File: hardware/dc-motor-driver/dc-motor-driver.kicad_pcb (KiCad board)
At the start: 2 copper layers, 73 parts, among them J1 VCC, J10 IMODE, J11 MOT, J12 IMODE, J13 MOT, J2 IMODE, J3 MOT, J4 IMODE, J5 MOT, J6 IMODE, J7 MOT, J8 IMODE, J9 MOT, U1 DRV8874PWPR, U2 DRV8874PWPR, U3 DRV8874PWPR, U4 DRV8874PWPR, U5 DRV8874PWPR, U6 DRV8874PWPR

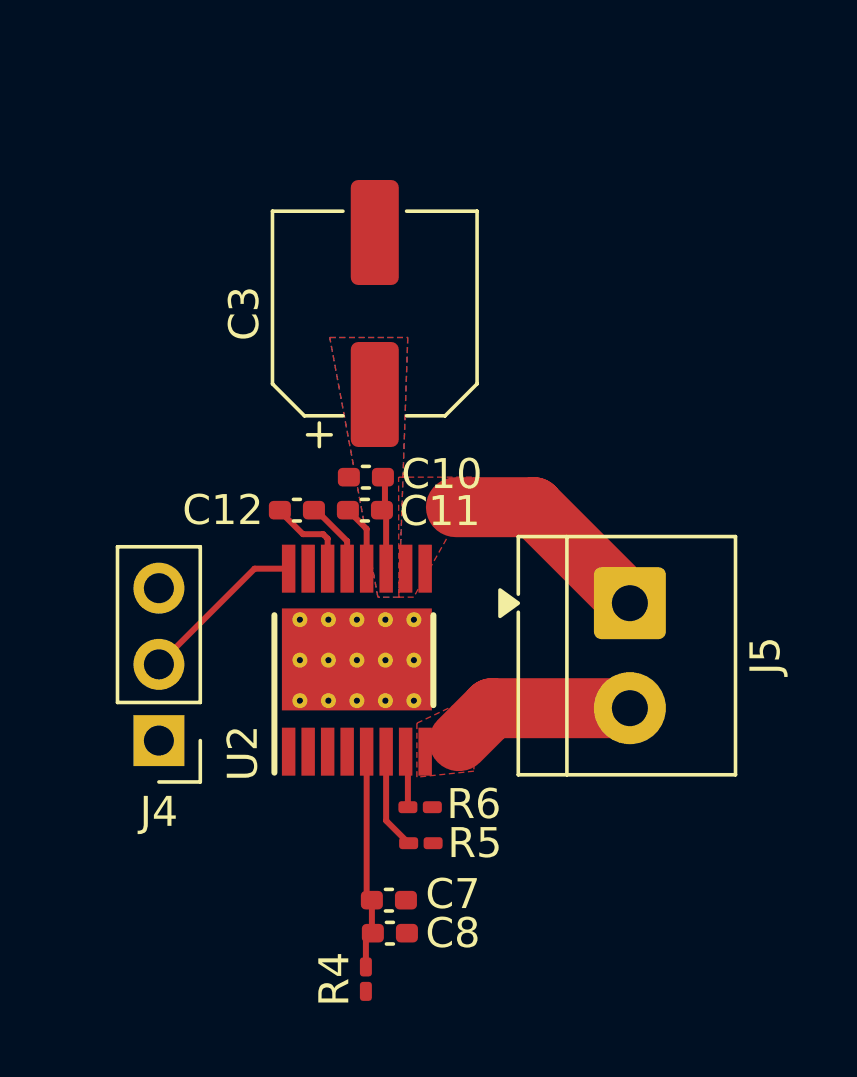
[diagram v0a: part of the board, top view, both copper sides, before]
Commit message: Replaced large current traces for copper pours and tweaked placement of components
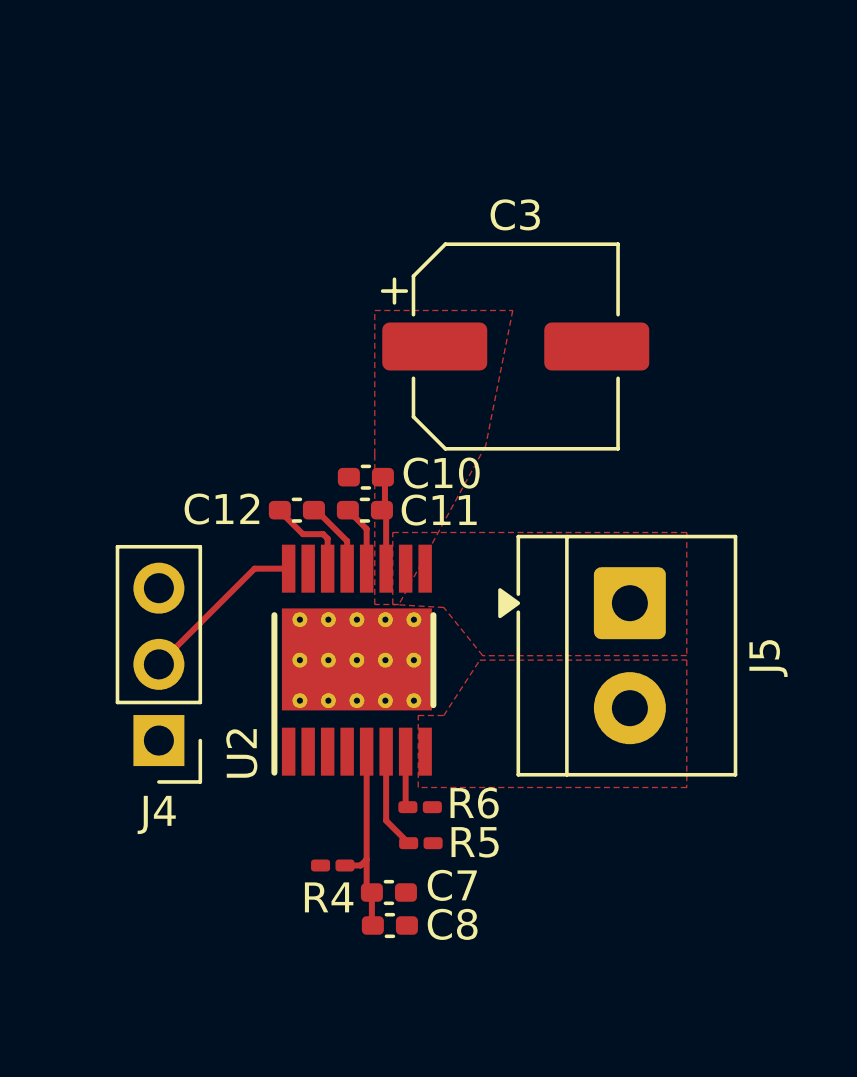
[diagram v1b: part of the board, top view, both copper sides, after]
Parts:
- moved C3 4.83 mm to (169.8, 77.5), turned to 0 degrees
- moved R4 3.95 mm to (163.7, 94.8), turned to 0 degrees
- moved C8 0.26 mm to (165.6, 96.8)
- moved C7 0.26 mm to (165.6, 95.7)
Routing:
- net Net-(J5-Pin_1): track 7.13 -> 0.00 mm
- net Net-(J5-Pin_2): track 6.16 -> 0.00 mm
- removed copper zone on B.Cu, net VCC

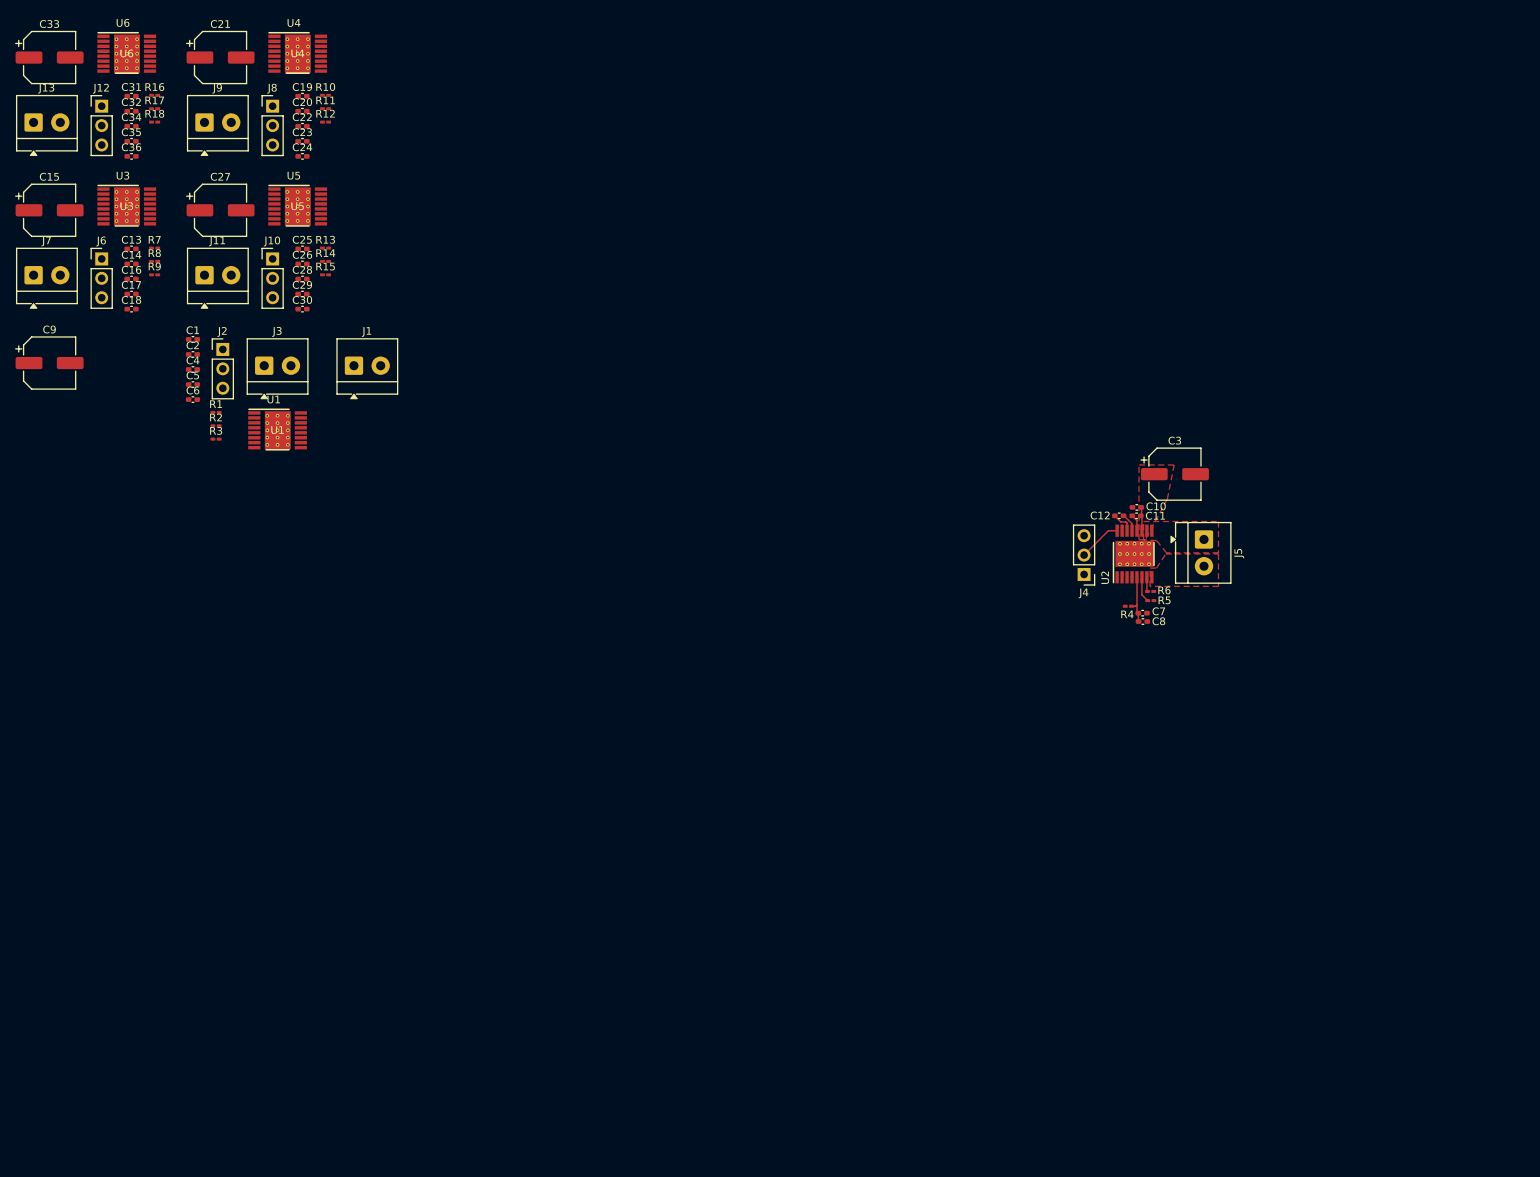
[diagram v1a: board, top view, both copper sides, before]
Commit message: feat: WIP PCB layout
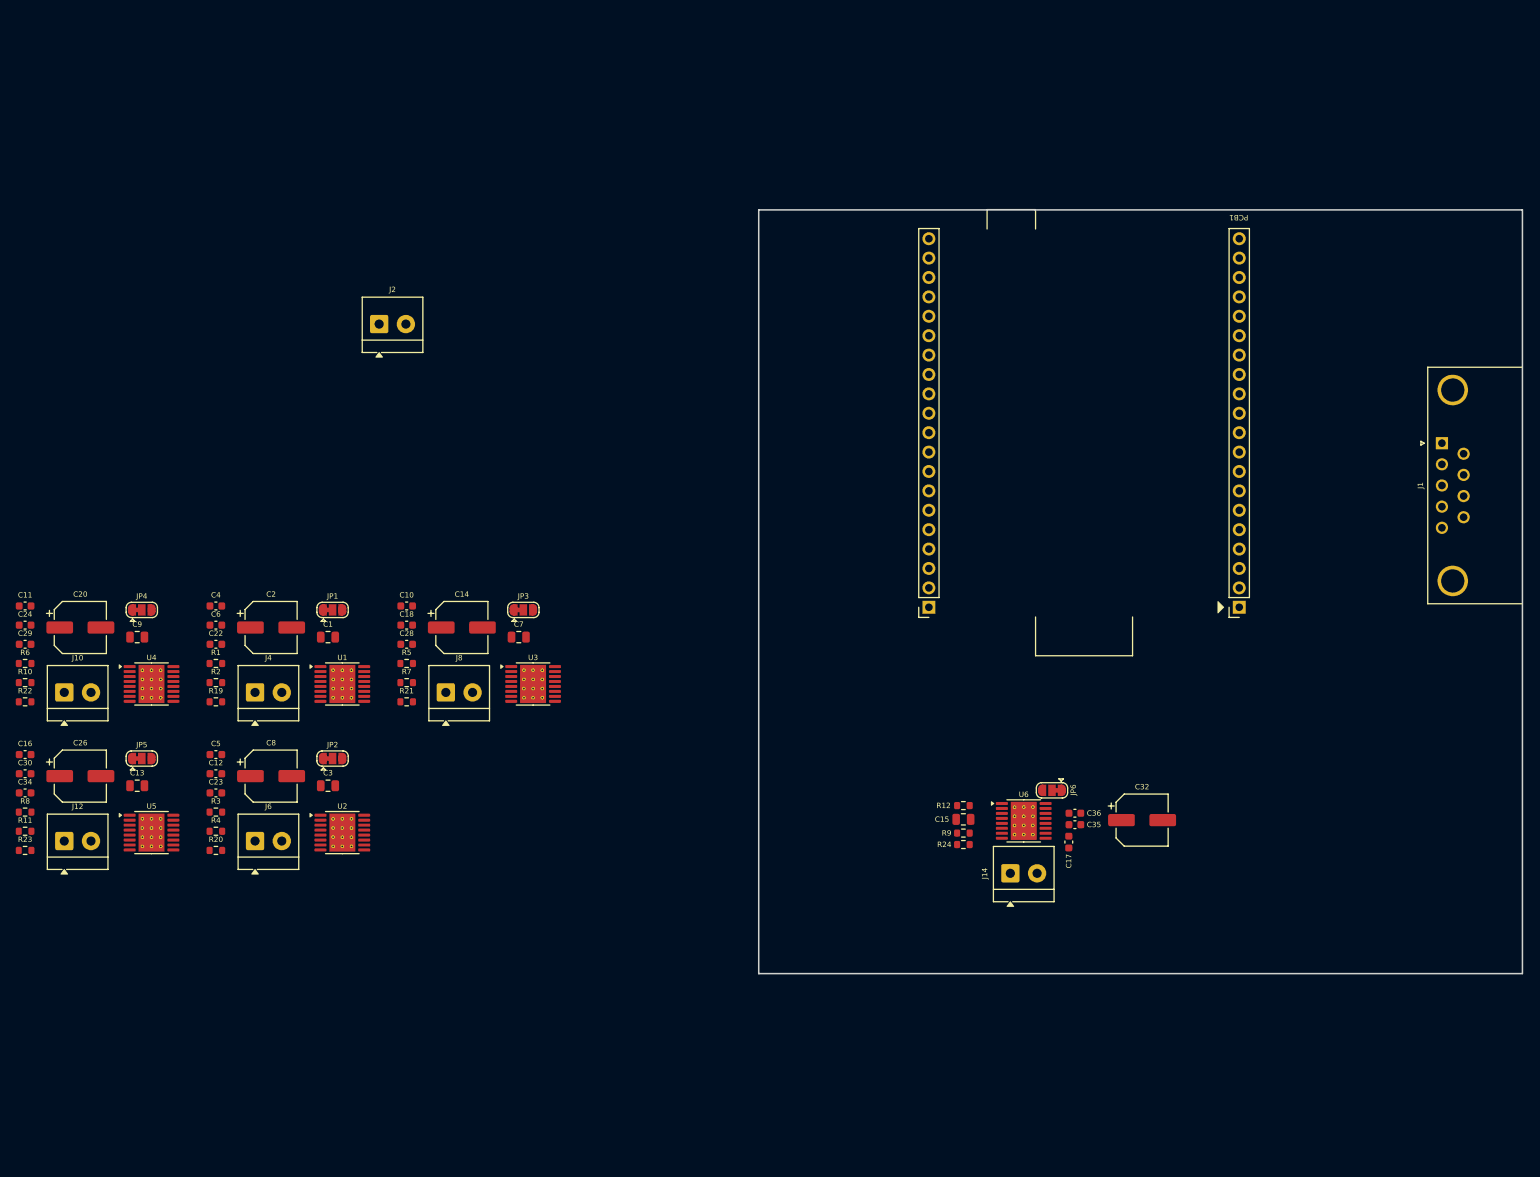
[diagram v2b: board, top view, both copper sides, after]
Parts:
- removed C19, C25, C31: 0.1uF, Capacitor_SMD:C_0402_1005Metric_Pad0.74x0.62mm_HandSolder
- removed C21, C27, C33: 100uF, Capacitor_SMD:CP_Elec_6.3x7.7
- removed J11, J13, J3, J5, J7, J9: MOT, TerminalBlock_4Ucon:TerminalBlock_4Ucon_1x02_P3.50mm_Horizontal
- removed R13, R16: 4.7k, Resistor_SMD:R_0201_0603Metric_Pad0.64x0.40mm_HandSolder
- removed R14, R17: 2.2k, Resistor_SMD:R_0201_0603Metric_Pad0.64x0.40mm_HandSolder
- removed R15, R18: 20k, Resistor_SMD:R_0201_0603Metric_Pad0.64x0.40mm_HandSolder
- added J14: MOT, TerminalBlock_4Ucon:TerminalBlock_4Ucon_1x02_P3.50mm_Horizontal, F.Cu at (148.2, 129.8)
- added JP1: Jumper_3_Bridged12, Jumper:SolderJumper-3_P1.3mm_Bridged12_RoundedPad1.0x1.5mm, F.Cu at (59.5, 95.3)
- added JP2: Jumper_3_Bridged12, Jumper:SolderJumper-3_P1.3mm_Bridged12_RoundedPad1.0x1.5mm, F.Cu at (59.5, 114.7)
- added JP3: Jumper_3_Bridged12, Jumper:SolderJumper-3_P1.3mm_Bridged12_RoundedPad1.0x1.5mm, F.Cu at (84.5, 95.3)
- added JP4: Jumper_3_Bridged12, Jumper:SolderJumper-3_P1.3mm_Bridged12_RoundedPad1.0x1.5mm, F.Cu at (34.5, 95.3)
- added JP5: Jumper_3_Bridged12, Jumper:SolderJumper-3_P1.3mm_Bridged12_RoundedPad1.0x1.5mm, F.Cu at (34.5, 114.7)
- added JP6: Jumper_3_Bridged12, Jumper:SolderJumper-3_P1.3mm_Bridged12_RoundedPad1.0x1.5mm, F.Cu at (153.7, 118.9)
- added PCB1: Smol Brain Board, Project PCB:Smol_Brain_Board, F.Cu at (157.9, 70.8)
- added R19: 20k, Resistor_SMD:R_0603_1608Metric, F.Cu at (44.2, 107.3)
- added R20: 20k, Resistor_SMD:R_0603_1608Metric, F.Cu at (44.2, 126.8)
- added R21: 20k, Resistor_SMD:R_0603_1608Metric, F.Cu at (69.2, 107.3)
- added R22: 20k, Resistor_SMD:R_0603_1608Metric, F.Cu at (19.2, 107.3)
- added R23: 20k, Resistor_SMD:R_0603_1608Metric, F.Cu at (19.2, 126.8)
- added R24: 20k, Resistor_SMD:R_0603_1608Metric, F.Cu at (142.1, 126.0)
- C1, C13, C7: value 0.1uF -> 10u; footprint Capacitor_SMD:C_0402_1005Metric_Pad0.74x0.62mm_HandSolder -> Capacitor_SMD:C_0805_2012Metric
- C10, C11, C16, C17, C22, C23, C28, C29, C34, C35, C4, C5: value 0.1uF -> 100n; footprint Capacitor_SMD:C_0402_1005Metric_Pad0.74x0.62mm_HandSolder -> Capacitor_SMD:C_0603_1608Metric
- C12, C18, C24, C30, C36, C6: value 0.022uF -> 22n; footprint Capacitor_SMD:C_0402_1005Metric_Pad0.74x0.62mm_HandSolder -> Capacitor_SMD:C_0603_1608Metric
- C14, C2, C20, C26, C32, C8: value 10uF -> 100u; footprint Capacitor_SMD:C_0402_1005Metric_Pad0.74x0.62mm_HandSolder -> Capacitor_SMD:CP_Elec_6.3x7.7
- C15, C3, C9: value 100uF -> 10u; footprint Capacitor_SMD:CP_Elec_6.3x7.7 -> Capacitor_SMD:C_0805_2012Metric
- J1: value VCC -> DE9; footprint TerminalBlock_4Ucon:TerminalBlock_4Ucon_1x02_P3.50mm_Horizontal -> THT:A-DF_09_A_KG-T2S
- J10, J12, J4, J6, J8: value IMODE -> MOT; footprint Connector_PinHeader_2.54mm:PinHeader_1x03_P2.54mm_Vertical -> TerminalBlock_4Ucon:TerminalBlock_4Ucon_1x02_P3.50mm_Horizontal
- J2: value IMODE -> VCC; footprint Connector_PinHeader_2.54mm:PinHeader_1x03_P2.54mm_Vertical -> TerminalBlock_4Ucon:TerminalBlock_4Ucon_1x02_P3.50mm_Horizontal
- R1, R10, R4, R7: value 4.7k -> 10k; footprint Resistor_SMD:R_0201_0603Metric_Pad0.64x0.40mm_HandSolder -> Resistor_SMD:R_0603_1608Metric
- R11: value 2.2k -> 10k; footprint Resistor_SMD:R_0201_0603Metric_Pad0.64x0.40mm_HandSolder -> Resistor_SMD:R_0603_1608Metric
- R12: value 20k -> 10k; footprint Resistor_SMD:R_0201_0603Metric_Pad0.64x0.40mm_HandSolder -> Resistor_SMD:R_0603_1608Metric
- R2, R5, R8: value 2.2k -> 2k2; footprint Resistor_SMD:R_0201_0603Metric_Pad0.64x0.40mm_HandSolder -> Resistor_SMD:R_0603_1608Metric
- R3, R6, R9: value 20k -> 2k2; footprint Resistor_SMD:R_0201_0603Metric_Pad0.64x0.40mm_HandSolder -> Resistor_SMD:R_0603_1608Metric
- U1, U2, U3, U4, U5, U6: footprint Package_DFN_QFN:DRV8874PWPR -> Package_SO:HTSSOP-16-1EP_4.4x5mm_P0.65mm_EP3.4x5mm_Mask2.66x2.46mm_ThermalVias
- moved C32 161.6 mm to (165.5, 122.8)
- moved U6 154.5 mm to (150.0, 122.9)
- moved C35 152.5 mm to (156.7, 123.4)
- moved C36 150.5 mm to (156.7, 121.9)
- moved R6 147.7 mm to (19.2, 102.3)
- moved C11 146.0 mm to (19.2, 94.8), turned to 0 degrees
- moved C15 143.8 mm to (142.1, 122.7), turned to 180 degrees
- moved J1 142.8 mm to (204.8, 73.4), turned to 90 degrees
- moved C17 142.2 mm to (155.9, 125.7), turned to -90 degrees
- moved R9 128.7 mm to (142.1, 124.5), turned to 180 degrees
- moved R4 123.1 mm to (44.2, 124.3)
- moved C12 123.0 mm to (44.2, 116.7), turned to 0 degrees
- moved R12 122.4 mm to (142.1, 120.9)
- moved C3 118.2 mm to (58.9, 118.3)
- moved C8 115.9 mm to (51.5, 117.0)
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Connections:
- net /nSLEEP renamed /~{SLEEP}
- C11 pad 2: Net-(U2-VCP) -> GND
- C13 pad 1: Net-(U3-VREF) -> Net-(U5-VREF)
- C14 pad 1: Net-(U3-VREF) -> VCC
- C15 pad 1: VCC -> Net-(U6-VREF)
- C17 pad 2: Net-(U3-VCP) -> GND
- C2 pad 1: Net-(U1-VREF) -> VCC
- C20 pad 1: Net-(U4-VREF) -> VCC
- C22 pad 2: GND -> Net-(U1-VCP)
- C23 pad 2: Net-(U4-VCP) -> Net-(U2-VCP)
- C26 pad 1: Net-(U5-VREF) -> VCC
- C28 pad 2: GND -> Net-(U3-VCP)
- C29 pad 2: Net-(U5-VCP) -> Net-(U4-VCP)
- C3 pad 1: VCC -> Net-(U2-VREF)
- C32 pad 1: Net-(U6-VREF) -> VCC
- C34 pad 2: GND -> Net-(U5-VCP)
- C5 pad 2: Net-(U1-VCP) -> GND
- C7 pad 1: Net-(U2-VREF) -> Net-(U3-VREF)
- C8 pad 1: Net-(U2-VREF) -> VCC
- C9 pad 1: VCC -> Net-(U4-VREF)
- J1 pad 1: GND -> Net-(PCB1-CAN_L)
- J1 pad 2: VCC -> Net-(PCB1-CAN_L)
- J10 pad 1: +3V3 -> Net-(J10-Pin_1)
- J12 pad 1: +3V3 -> Net-(J12-Pin_1)
- J2 pad 1: +3V3 -> GND
- J2 pad 2: Net-(J2-Pin_2) -> VCC
- J4 pad 1: +3V3 -> Net-(J4-Pin_1)
- J6 pad 1: +3V3 -> Net-(J6-Pin_1)
- J8 pad 1: +3V3 -> Net-(J8-Pin_1)
- R1 pad 1: /ILIM -> /BANK1_ILIM
- R10 pad 1: /ILIM -> /BANK2_ILIM
- R11 pad 1: GND -> /Driver_5/I_LIM
- R11 pad 2: /MotorDriver4/MOT_ISENSE -> Net-(U5-VREF)
- R12 pad 1: Net-(U4-IMODE) -> /Driver_6/I_LIM
- R12 pad 2: GND -> Net-(U6-VREF)
- R2 pad 1: GND -> /BANK1_I_SENSE
- R2 pad 2: /MotorDriver1/MOT_ISENSE -> GND
- R3 pad 1: Net-(U1-IMODE) -> /BANK1_I_SENSE
- R4 pad 1: /ILIM -> /BANK1_ILIM
- R5 pad 1: GND -> /BANK2_I_SENSE
- R5 pad 2: /MotorDriver2/MOT_ISENSE -> GND
- R6 pad 1: Net-(U2-IMODE) -> /BANK2_I_SENSE
- R7 pad 1: /ILIM -> /BANK2_ILIM
- R8 pad 1: GND -> /BANK3_I_SENSE
- R8 pad 2: /MotorDriver3/MOT_ISENSE -> GND
- R9 pad 1: Net-(U3-IMODE) -> /BANK3_I_SENSE
- U1 pad 1: /MotorDriver1/MOT_IN1 -> /MOT1_IN1
- U1 pad 10: Net-(J3-Pin_1) -> Net-(J4-Pin_2)
- U1 pad 16: Net-(J2-Pin_2) -> Net-(JP1-C)
- U1 pad 2: /MotorDriver1/MOT_IN2 -> /MOT1_IN2
- U1 pad 4: /nFAULT -> /BANK1_~{FLT}
- U1 pad 6: /MotorDriver1/MOT_ISENSE -> /BANK1_I_SENSE
- U1 pad 8: Net-(J3-Pin_2) -> Net-(J4-Pin_1)
- U2 pad 1: /MotorDriver2/MOT_IN1 -> /MOT2_IN1
- U2 pad 10: Net-(J5-Pin_1) -> Net-(J6-Pin_2)
- U2 pad 16: Net-(J4-Pin_2) -> Net-(JP2-C)
- U2 pad 2: /MotorDriver2/MOT_IN2 -> /MOT2_IN2
- U2 pad 4: /nFAULT -> /BANK1_~{FLT}
- U2 pad 6: /MotorDriver2/MOT_ISENSE -> /BANK1_I_SENSE
- U2 pad 8: Net-(J5-Pin_2) -> Net-(J6-Pin_1)
- U3 pad 1: /MotorDriver3/MOT_IN1 -> /MOT3_IN1
- U3 pad 10: Net-(J7-Pin_1) -> Net-(J8-Pin_2)
- U3 pad 16: Net-(J6-Pin_2) -> Net-(JP3-C)
- U3 pad 2: /MotorDriver3/MOT_IN2 -> /MOT3_IN2
- U3 pad 4: /nFAULT -> /BANK2_~{FLT}
- U3 pad 6: /MotorDriver3/MOT_ISENSE -> /BANK2_I_SENSE
- U3 pad 8: Net-(J7-Pin_2) -> Net-(J8-Pin_1)
- U4 pad 1: /MotorDriver4/MOT_IN1 -> /MOT4_IN1
- U4 pad 10: Net-(J9-Pin_1) -> Net-(J10-Pin_2)
- U4 pad 16: Net-(J8-Pin_2) -> Net-(JP4-C)
- U4 pad 2: /MotorDriver4/MOT_IN2 -> /MOT4_IN2
- U4 pad 4: /nFAULT -> /BANK2_~{FLT}
- U4 pad 6: /MotorDriver4/MOT_ISENSE -> /BANK2_I_SENSE
- U4 pad 8: Net-(J9-Pin_2) -> Net-(J10-Pin_1)
- U5 pad 1: /MotorDriver5/MOT_IN1 -> /MOT5_IN1
- U5 pad 10: Net-(J11-Pin_1) -> Net-(J12-Pin_2)
- U5 pad 16: Net-(J10-Pin_2) -> Net-(JP5-C)
- U5 pad 2: /MotorDriver5/MOT_IN2 -> /MOT5_IN2
- U5 pad 4: /nFAULT -> /BANK3_~{FLT}
- U5 pad 6: /MotorDriver5/MOT_ISENSE -> /BANK3_I_SENSE
- U5 pad 8: Net-(J11-Pin_2) -> Net-(J12-Pin_1)
- U6 pad 1: /MotorDriver6/MOT_IN1 -> /MOT6_IN1
- U6 pad 16: Net-(J12-Pin_2) -> Net-(JP6-C)
- U6 pad 2: /MotorDriver6/MOT_IN2 -> /MOT6_IN2
- U6 pad 4: /nFAULT -> /BANK3_~{FLT}
- U6 pad 6: /MotorDriver6/MOT_ISENSE -> /BANK3_I_SENSE
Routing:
- net Net-(U2-VREF): track 6.97 -> 0.00 mm
- net Net-(J4-Pin_2): track 5.65 -> 0.00 mm
- net /MotorDriver2/MOT_ISENSE: track 3.36 -> 0.00 mm
- net Net-(U2-CPL): track 2.88 -> 0.00 mm
- net VCC: track 2.87 -> 0.00 mm
- net Net-(U2-CPH): track 2.34 -> 0.00 mm
- net Net-(U2-VCP): track 2.07 -> 0.00 mm
- net Net-(U2-IMODE): track 1.99 -> 0.00 mm
- removed copper zone on F.Cu, net Net-(J5-Pin_1)
- removed copper zone on F.Cu, net Net-(J5-Pin_2)
- removed copper zone on F.Cu, net VCC
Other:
- board outline added: 100 x 100 mm
